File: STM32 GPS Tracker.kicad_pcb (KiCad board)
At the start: 4 copper layers, 43.5 x 58.5 mm, 57 parts, among them J1 Screw_Terminal_01x02, J2 LEFT HEADER PINS, J3 693010020611, J4 RIGHT HEADER PINS, Q1 AO3407A, SW1 SW_Push, SW2 SW_Push, U1 SIM808, U2 TPS5430DDA, U3 SMF05CT1G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

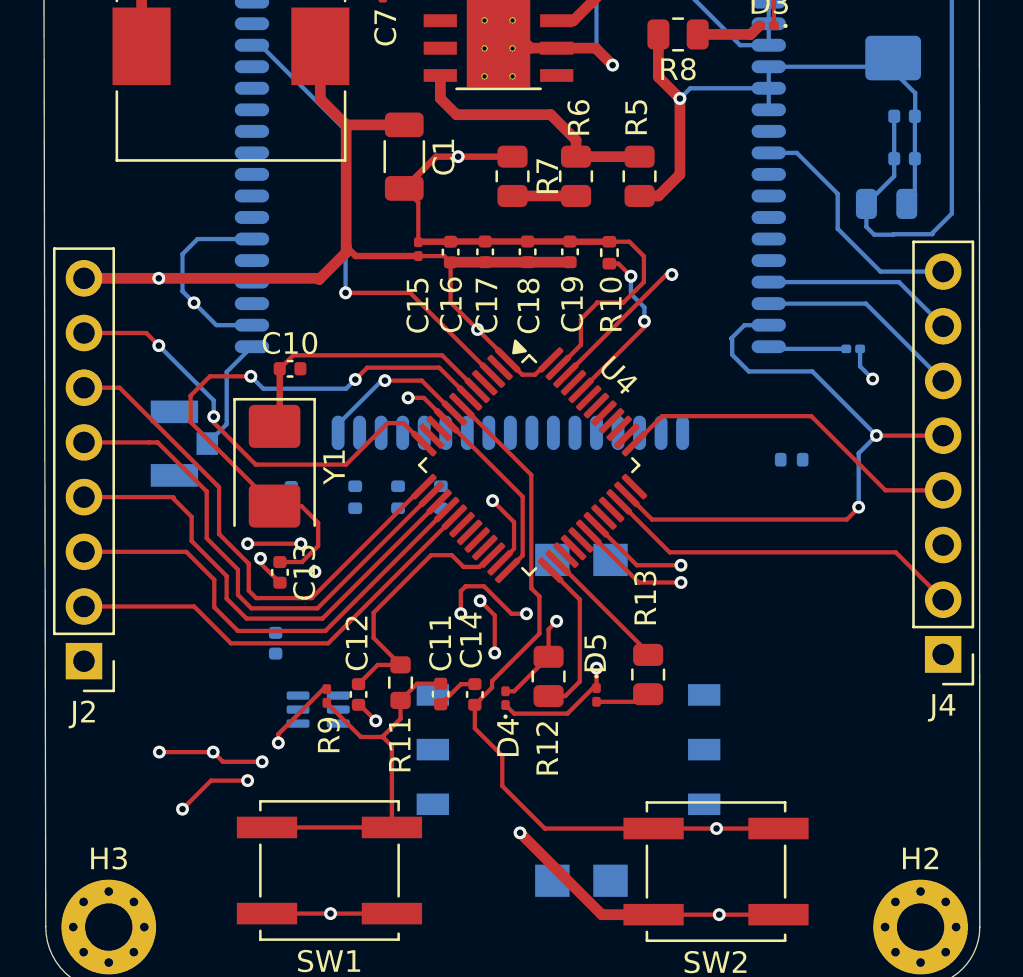
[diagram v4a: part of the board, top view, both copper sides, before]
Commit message: Remaining Tracks for Back Copper Layer (In Progress)
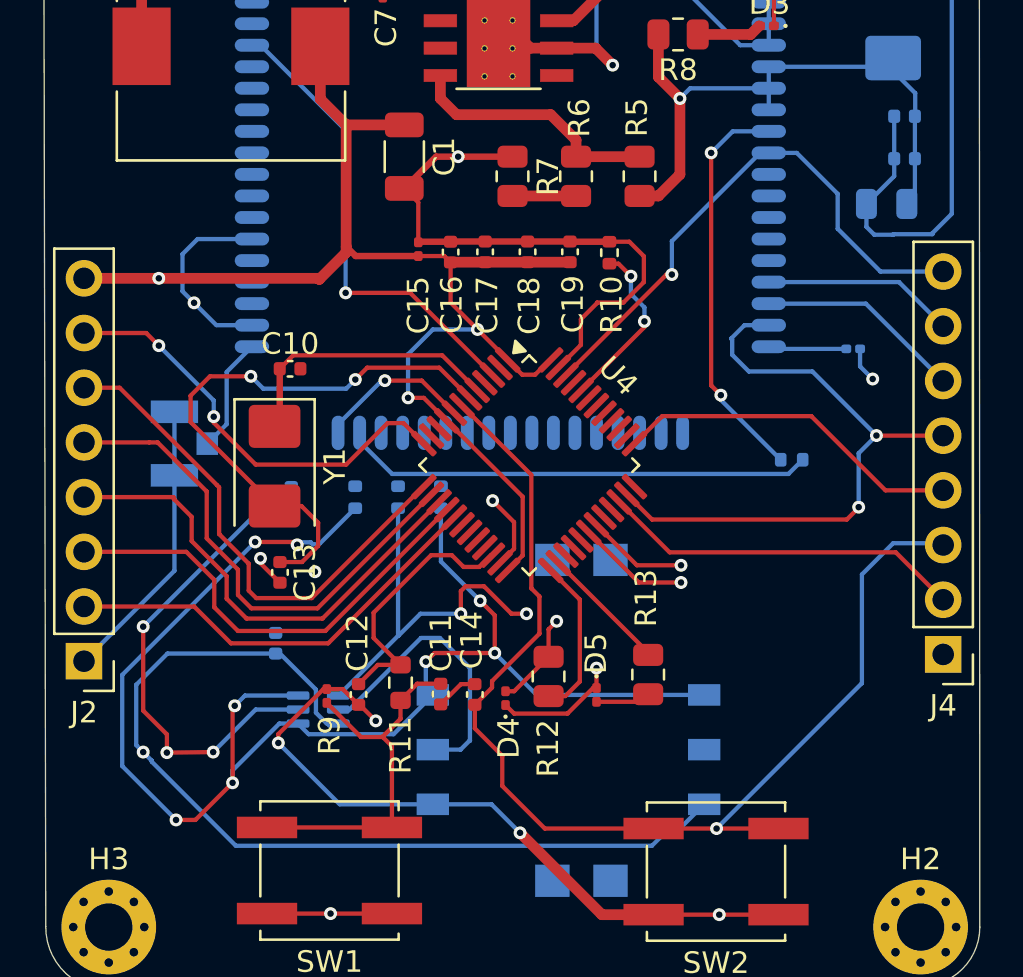
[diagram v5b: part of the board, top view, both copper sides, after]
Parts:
- turned U3 to 0 degrees
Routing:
- net Net-(J3-CLK): track 0.00 -> 67.1 mm, vias 0 -> 8
- net SIM_VDD: track 0.00 -> 43.9 mm, vias 0 -> 1
- net SIM_DET: track 0.00 -> 35.2 mm
- net GND: track 193.9 -> 221.9 mm
- net Net-(C6-Pad2): track 0.00 -> 22.4 mm, vias 0 -> 3
- net NRST: track 34.6 -> 53.6 mm
- net Net-(U1-VDD_EXT): track 0.00 -> 18.7 mm, vias 0 -> 2
- net (no net): track 18.4 -> 0.00 mm, vias 12 -> 1
- net Net-(J3-RET): track 0.00 -> 17.9 mm, vias 0 -> 2
- net SIM_PWRKEY: track 18.2 -> 25.9 mm
- net +3.3V: track 90.0 -> 95.7 mm
